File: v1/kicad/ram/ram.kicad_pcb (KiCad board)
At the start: 2 copper layers, 67 x 74.5 mm, 3 parts, among them IC1 AS6C6264-55PCN, U1 LNCPU Type A Connector, U2 74LS32

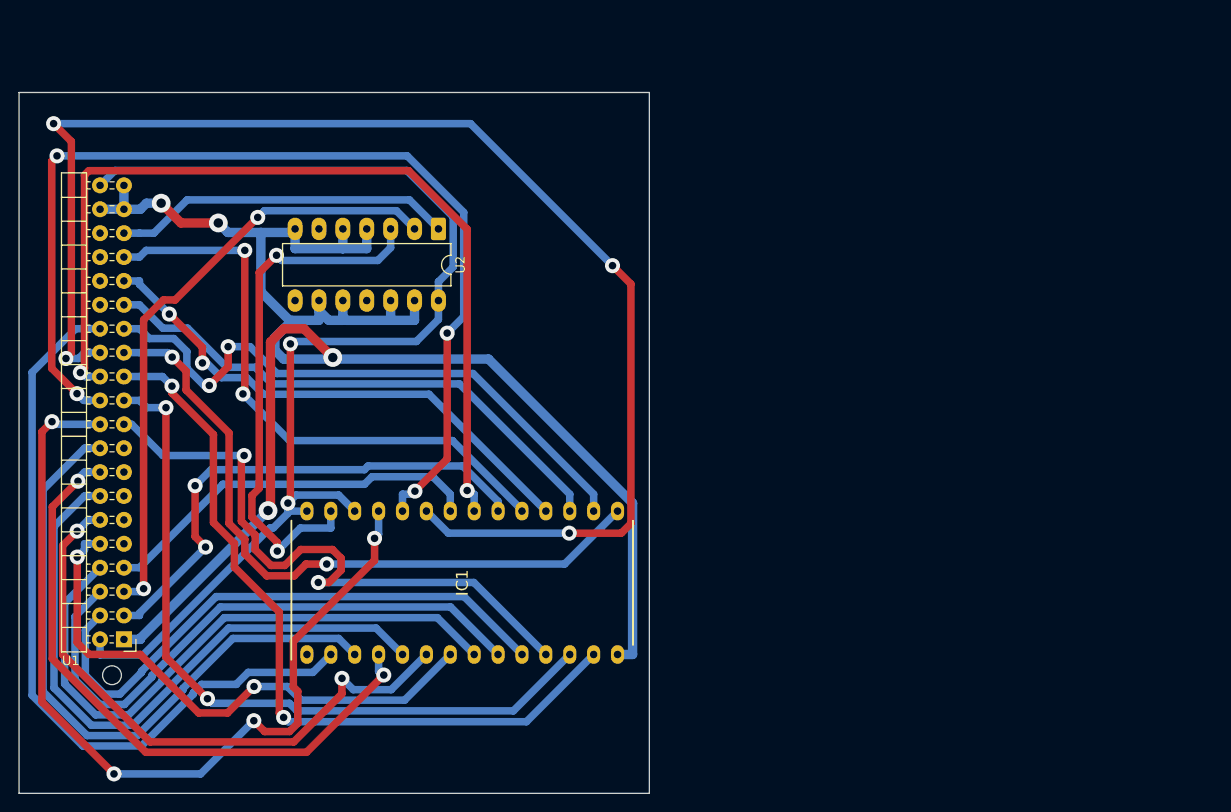
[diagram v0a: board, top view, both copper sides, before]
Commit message: readapt designs for BR, SP, SR, ALU
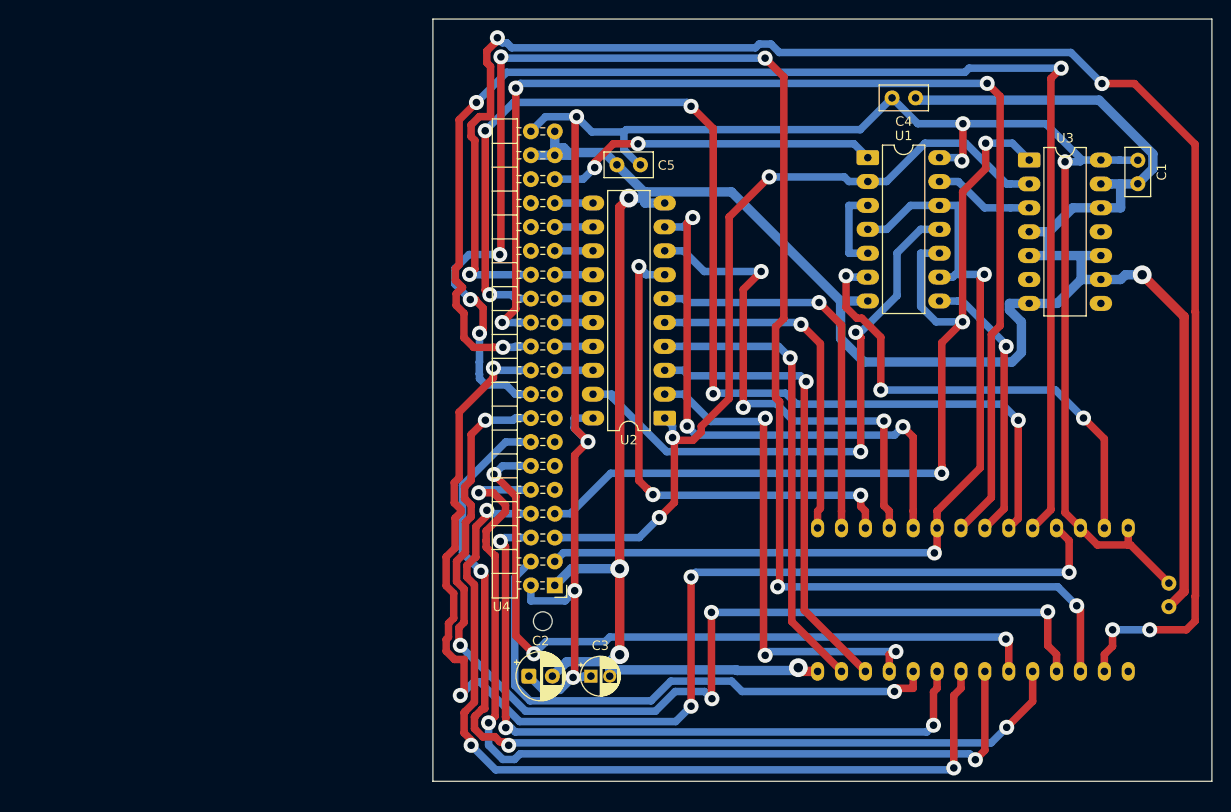
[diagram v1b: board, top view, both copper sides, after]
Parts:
- added C1: 220n, Capacitor_THT:C_Disc_D5.0mm_W2.5mm_P2.50mm, F.Cu at (201.4, 45.7)
- added C2: 47u, Capacitor_THT:CP_Radial_D5.0mm_P2.50mm, F.Cu at (136.7, 98.0)
- added C3: 1u, lncpu:CP_Radial_D4.0mm_P2.00mm-Large-Holes, F.Cu at (143.3, 98.0)
- added C4: 220n, Capacitor_THT:C_Disc_D5.0mm_W2.5mm_P2.50mm, F.Cu at (177.8, 36.6)
- added C5: 100n, Capacitor_THT:C_Disc_D5.0mm_W2.5mm_P2.50mm, F.Cu at (146.1, 43.7)
- added C6: 100n, Capacitor_THT:C_Disc_D5.0mm_W2.5mm_P2.50mm, B.Cu at (204.7, 90.7)
- added U3: 74HCT08, Package_DIP:DIP-14_W7.62mm_LongPads, F.Cu at (189.9, 43.2)
- added U4: LNCPU Type A Header, lncpu:LNCPU_Type_A_Header, F.Cu at (139.4, 88.4)
- IC1: moved to B.Cu
- U1: value LNCPU Type A Connector -> 74HCT32; footprint lncpu:LNCPU_Type_A_Header -> Package_DIP:DIP-14_W7.62mm_LongPads
- U2: value 74LS32 -> 74HCT245; footprint Package_DIP:DIP-14_W7.62mm_LongPads -> Package_DIP:DIP-20_W7.62mm_LongPads
- moved U1 94.2 mm to (172.7, 42.9), turned to 0 degrees
- moved IC1 54.3 mm to (183.9, 89.9)
- moved U2 31.4 mm to (151.1, 70.6), turned to 180 degrees
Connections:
- IC1 pad 20: Net-(IC1-~{CE_{1}}) -> /~{RAM_{sel}}
- U1 pad 1: GND -> /~{CLK}
- U1 pad 10: /ABUS3 -> /~{DEV_{out}}
- U1 pad 11: unconnected-(U1-CTRL_{4}-Pad11) -> Net-(U2-CE)
- U1 pad 12: /ABUS4 -> /~{RAM_{sel}}
- U1 pad 13: unconnected-(U1-CTRL_{5}-Pad13) -> Net-(U1-Pad13)
- U1 pad 14: /ABUS5 -> VCC
- U1 pad 2: VCC -> /~{DEV_{in}}
- U1 pad 3: Net-(IC1-~{CE_{1}}) -> Net-(U1-Pad3)
- U1 pad 4: /ABUS0 -> /~{RAM_{sel}}
- U1 pad 5: Net-(U1-CTRL_{1}) -> Net-(U1-Pad3)
- U1 pad 6: /ABUS1 -> Net-(IC1-~{WE})
- U1 pad 7: Net-(IC1-~{OE}) -> GND
- U1 pad 8: /ABUS2 -> Net-(IC1-~{OE})
- U1 pad 9: unconnected-(U1-CTRL_{3}-Pad9) -> /~{RAM_{sel}}
- U2 pad 1: Net-(U1-CLK1) -> /~{DEV_{in}}
- U2 pad 11: unconnected-(U2-Pad11) -> Net-(U2-B7)
- U2 pad 12: GND -> Net-(U2-B6)
- U2 pad 13: GND -> Net-(U2-B5)
- U2 pad 14: VCC -> Net-(U2-B4)
- U2 pad 2: Net-(U1-CTRL_{1}) -> /DBUS0
- U2 pad 3: Net-(IC1-~{WE}) -> /DBUS1
- U2 pad 4: GND -> /DBUS2
- U2 pad 5: GND -> /DBUS3
- U2 pad 6: unconnected-(U2-Pad6) -> /DBUS4
- U2 pad 7: GND -> /DBUS5
- U2 pad 8: unconnected-(U2-Pad8) -> /DBUS6
- U2 pad 9: GND -> /DBUS7
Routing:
- net /ABUS7: track 69.5 -> 171.6 mm, vias 0 -> 7
- net /~{DEV_{out}}: track 0.00 -> 101.2 mm, vias 0 -> 3
- net GND: track 185.8 -> 285.0 mm, vias 4 -> 5
- net /ABUS12: track 81.6 -> 178.1 mm, vias 0 -> 5
- net /~{RAM_{sel}}: track 0.00 -> 95.5 mm, vias 0 -> 2
- net VCC: track 124.8 -> 216.7 mm, vias 2 -> 7
- net /~{DEV_{in}}: track 0.00 -> 88.3 mm, vias 0 -> 3
- net Net-(U1-CTRL_{1}): track 65.2 -> 0.00 mm, vias 2 -> 0
- net Net-(U2-CE): track 0.00 -> 63.2 mm, vias 0 -> 2
- net Net-(IC1-~{CE_{1}}): track 54.5 -> 0.00 mm, vias 2 -> 0
- net /ABUS6: track 68.2 -> 113.9 mm, vias 2 -> 5
- net /ABUS3: track 59.0 -> 99.3 mm, vias 2 -> 3
- net /ABUS9: track 110.1 -> 148.3 mm, vias 4 -> 3
- net Net-(U1-CLK1): track 36.2 -> 0.00 mm
- net /~{CLK}: track 0.00 -> 35.8 mm, vias 0 -> 2
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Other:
- board size 67 x 74.5 mm -> 82.8 x 81 mm
